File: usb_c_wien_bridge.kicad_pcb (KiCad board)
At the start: 2 copper layers, 49 x 14 mm, 20 parts, among them J1 USB_C_Receptacle_USB2.0, J2 Conn_01x05_Female, U1 TL082

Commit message: Place all components. Needs routing.
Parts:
- added C10: 47uF, Capacitor_SMD:CP_Elec_6.3x5.4_Nichicon, F.Cu at (193.0, 17.8)
- added C11: 1uF, Capacitor_SMD:C_0603_1608Metric_Pad1.05x0.95mm_HandSolder, B.Cu at (183.1, 22.0)
- added C12: 1uF, Capacitor_SMD:C_0603_1608Metric_Pad1.05x0.95mm_HandSolder, B.Cu at (183.1, 20.4)
- added C9: 1nF, Capacitor_SMD:C_0603_1608Metric_Pad1.05x0.95mm_HandSolder, B.Cu at (185.3, 13.5)
- added J3: Conn_02x02, Connector_PinSocket_2.00mm:PinSocket_2x02_P2.00mm_Horizontal, F.Cu at (177.8, 20.9)
- added U2: MIC5504-3.3YM5, Package_TO_SOT_SMD:SOT-23-5, B.Cu at (171.6, 17.1)
- C1, C2, D1, D2, R1, R2, R3, R4, R5, R6, R7: moved to B.Cu
- C3: value 0u1F -> 1uF; footprint Capacitor_SMD:C_0603_1608Metric -> Capacitor_SMD:C_0603_1608Metric_Pad1.05x0.95mm_HandSolder; moved to B.Cu
- C4: footprint Capacitor_SMD:C_0603_1608Metric_Pad1.05x0.95mm_HandSolder -> Capacitor_SMD:C_0603_1608Metric; moved to B.Cu
- C5: value 1nF -> 0u1F; moved to B.Cu
- C6: value 1nF -> 1uF; moved to B.Cu
- C7: value 47uF -> 0u1F; footprint Capacitor_SMD:CP_Elec_6.3x5.4_Nichicon -> Capacitor_SMD:C_0603_1608Metric; moved to B.Cu
- C8: value 1uF -> 1nF; moved to B.Cu
- J1: footprint Connector_USB:USB_C_Receptacle_Amphenol_12401610E4-2A -> Amphenol:USB_C_Receptacle_Amphenol_12401610E4-2A
- J2: value Conn_01x05_Female -> Screw_Terminal_01x02; footprint Connector_PinSocket_2.54mm:PinSocket_1x05_P2.54mm_Horizontal -> TerminalBlock_TE-Connectivity:TerminalBlock_TE_282834-2_1x02_P2.54mm_Horizontal
- U1: value TL082 -> LMV358; footprint Package_SO:SOIC-8_3.9x4.9mm_P1.27mm -> Package_SO:TSSOP-8_4.4x3mm_P0.65mm; moved to B.Cu
- moved C4 154.2 mm to (169.3, 20.6), turned to 270 degrees
- moved C6 146.7 mm to (171.8, 19.8), turned to 180 degrees
- moved C5 140.4 mm to (186.1, 21.5), turned to 270 degrees
- moved R2 134.5 mm to (179.1, 16.9), turned to 180 degrees
- moved C3 134.0 mm to (187.7, 21.5), turned to 270 degrees
- moved R4 133.5 mm to (185.3, 15.1), turned to 180 degrees
- moved R1 132.8 mm to (179.1, 18.5)
- moved C1 131.3 mm to (189.4, 21.5), turned to 270 degrees
- moved D1 131.2 mm to (193.2, 17.7), turned to 270 degrees
- moved R3 130.1 mm to (191.1, 14.2), turned to 90 degrees
- moved C8 129.2 mm to (187.8, 14.2), turned to 270 degrees
- moved R6 125.4 mm to (189.5, 14.2), turned to 90 degrees
- moved C2 125.2 mm to (168.8, 17.3), turned to 90 degrees
- moved R7 122.8 mm to (191.0, 22.5), turned to 270 degrees
- moved R5 122.3 mm to (189.9, 17.7), turned to 90 degrees
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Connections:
- net Net-(D1-Pad1) renamed /NEG_FB
- C1 pad 1: +5V0 -> +3V3
- C3 pad 1: +5V0 -> +3V3
- C4 pad 1: Net-(C4-Pad1) -> +5V0
- C5 pad 1: Net-(C5-Pad1) -> /V_DIV
- C5 pad 2: Net-(C5-Pad2) -> GNDA
- C6 pad 1: /RAIL_SPLIT -> +3V3
- C6 pad 2: Net-(C5-Pad2) -> GNDA
- C7 pad 1: Net-(C7-Pad1) -> +3V3
- C7 pad 2: Net-(C7-Pad2) -> GNDA
- C8 pad 1: +5V0 -> Net-(C8-Pad1)
- C8 pad 2: GNDA -> /POS_FB
- D1 pad 2: Net-(C7-Pad1) -> Net-(C10-Pad1)
- D2 pad 1: Net-(C7-Pad1) -> Net-(C10-Pad1)
- J1 pad A5: (no net) -> Net-(J1-PadA5)
- J1 pad A6: (no net) -> Net-(J1-PadA6)
- J1 pad A7: (no net) -> Net-(J1-PadA7)
- J1 pad A8: (no net) -> Net-(J1-PadA8)
- J1 pad B5: (no net) -> Net-(J1-PadB5)
- J1 pad B6: (no net) -> Net-(J1-PadB6)
- J1 pad B7: (no net) -> Net-(J1-PadB7)
- J1 pad B8: (no net) -> Net-(J1-PadB8)
- J2 pad 1: GNDA -> Net-(J2-Pad1)
- J2 pad 2: Net-(C7-Pad2) -> +5V0
- R1 pad 1: +5V0 -> +3V3
- R1 pad 2: Net-(C4-Pad1) -> /V_DIV
- R2 pad 1: Net-(C4-Pad1) -> /V_DIV
- R4 pad 1: Net-(C5-Pad2) -> /POS_FB
- R5 pad 1: Net-(C7-Pad1) -> Net-(C10-Pad1)
- R6 pad 1: Net-(C7-Pad1) -> Net-(C10-Pad1)
- R6 pad 2: Net-(C5-Pad1) -> Net-(C8-Pad1)
- R7 pad 1: Net-(C7-Pad2) -> /A_OUT
- U1 pad 2: Net-(C4-Pad1) -> /RAIL_SPLIT
- U1 pad 3: GNDA -> /V_DIV
- U1 pad 5: Net-(C5-Pad2) -> /POS_FB
- U1 pad 7: Net-(C7-Pad1) -> Net-(C10-Pad1)
- U1 pad 8: +5V0 -> +3V3
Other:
- board size 49 x 14 mm -> 31.8 x 12.7 mm

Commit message: Finish routing
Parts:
- R7: moved to F.Cu
- moved C10 91.8 mm to (146.7, 97.0), turned to 180 degrees
- moved R7 91.4 mm to (137.4, 96.5), turned to 180 degrees
- moved C12 89.5 mm to (142.7, 100.3)
- moved J3 87.9 mm to (137.4, 99.0)
- moved C2 87.9 mm to (128.4, 95.4)
- moved C4 87.9 mm to (128.9, 98.7)
- moved C6 87.9 mm to (131.4, 97.9)
- moved J1 87.9 mm to (129.8, 95.9)
- moved J2 87.9 mm to (140.6, 91.8)
- moved R1 87.9 mm to (138.7, 96.6)
- moved R4 87.9 mm to (144.9, 93.2)
- moved U1 87.9 mm to (144.7, 95.9)
- moved U2 87.9 mm to (131.2, 95.2)
- moved C1 87.9 mm to (149.0, 99.6)
- moved C3 87.9 mm to (147.3, 99.6)
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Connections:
- J3 pad 1: GNDA -> /A_OUT
- J3 pad 2: /A_OUT -> GNDA
- J3 pad 3: +3V3 -> +5V0
- J3 pad 4: +5V0 -> +3V3
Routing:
- net +3V3: track 0.00 -> 36.0 mm
- net GNDA: track 0.00 -> 31.9 mm, vias 0 -> 8
- net +5V0: track 0.00 -> 31.6 mm, vias 0 -> 2
- net Net-(C10-Pad1): track 0.00 -> 22.2 mm, vias 0 -> 2
- net /RAIL_SPLIT: track 0.00 -> 14.7 mm
- net Net-(J2-Pad1): track 0.00 -> 13.7 mm
- net /V_DIV: track 0.00 -> 10.8 mm
- net /A_OUT: track 0.00 -> 8.55 mm
- net /NEG_FB: track 0.00 -> 7.18 mm
- net /POS_FB: track 0.00 -> 5.09 mm
- net Net-(C8-Pad1): track 0.00 -> 1.65 mm
- added copper zone on B.Cu, net GNDA
- added copper zone on F.Cu, net GNDA
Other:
- net class OSH Park Minimums added: clearance 0.1524, trace_width 0.1524, via_dia 0.508, via_drill 0.254
- rule pad_to_mask_clearance: 0.051 -> 0.0508
- rule solder_mask_min_width: 0.25 -> 0.1016
- rule trace_min: 0.2 -> 0.1524
- rule via_min_drill: 0.3 -> 0.254
- rule via_min_size: 0.4 -> 0.508

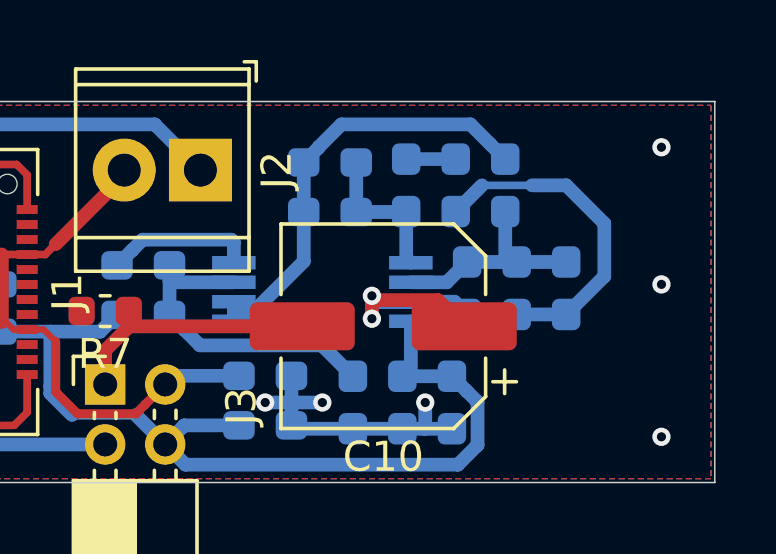
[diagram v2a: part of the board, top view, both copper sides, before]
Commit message: Add vias to ground islands
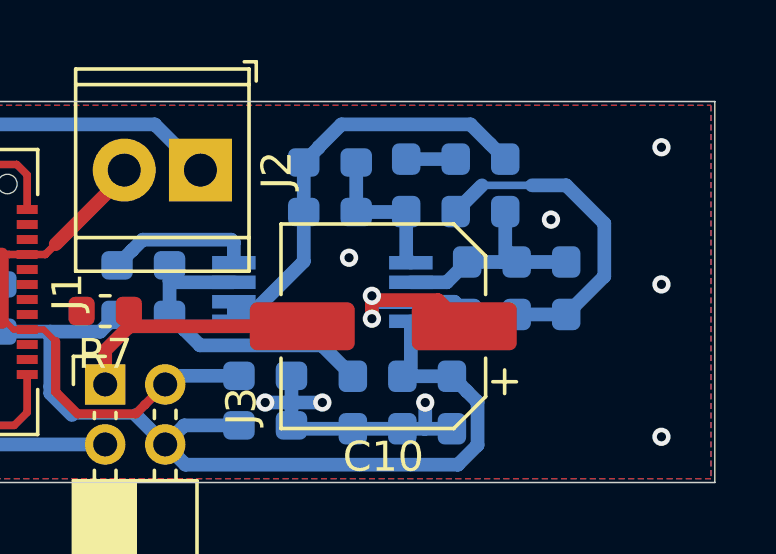
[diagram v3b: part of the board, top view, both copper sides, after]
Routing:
- net GNDA: vias 8 -> 10
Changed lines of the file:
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@@
     (thickness 1.6)
     (drawings 4)
-    (tracks 177)
+    (tracks 179)
     (zones 0)
     (modules 26)
@@
   )
   (setup
-    (last_trace_width 0.3048)
+    (last_trace_width 0.25)
     (user_trace_width 0.1524)
     (user_trace_width 0.2032)
@@
   (gr_line (start 157.734 89.535) (end 157.734 102.235) (layer Edge.Cuts) (width 0.05))
   (gr_line (start 125.984 89.535) (end 157.734 89.535) (layer Edge.Cuts) (width 0.05))
+  (via (at 152.273 93.472) (size 0.6096) (drill 0.3048) (layers F.Cu B.Cu) (net 1))
+  (via (at 145.542 94.742) (size 0.6096) (drill 0.3048) (layers F.Cu B.Cu) (net 1))
   (via (at 128.397 93.345) (size 0.6096) (drill 0.3048) (layers F.Cu B.Cu) (net 1))
   (via (at 127.254 94.488) (size 0.6096) (drill 0.3048) (layers F.Cu B.Cu) (net 1))
@@
   (via (at 131.191 94.869) (size 0.6096) (drill 0.3048) (layers F.Cu B.Cu) (net 2))
   (via (at 131.191 95.631) (size 0.6096) (drill 0.3048) (layers F.Cu B.Cu) (net 2))
-  (via (at 146.304 96.774) (size 0.6096) (drill 0.3048) (layers F.Cu B.Cu) (net 6))
-  (via (at 146.304 96.012) (size 0.6096) (drill 0.3048) (layers F.Cu B.Cu) (net 6))
   (segment (start 130.025 96.266) (end 130.091 96.2) (width 0.4572) (layer B.Cu) (net 2))
   (segment (start 128.905 97.8915) (end 128.905 96.266) (width 0.4572) (layer B.Cu) (net 2))
@@
   (segment (start 138.434199 99.985199) (end 136.307199 99.985199) (width 0.3048) (layer B.Cu) (net 4))
   (segment (start 149.098 91.454) (end 147.447 91.454) (width 0.4572) (layer B.Cu) (net 5))
+  (via (at 146.304 96.774) (size 0.6096) (drill 0.3048) (layers F.Cu B.Cu) (net 6))
+  (via (at 146.304 96.012) (size 0.6096) (drill 0.3048) (layers F.Cu B.Cu) (net 6))
   (segment (start 149.056 96.21) (end 149.479 96.633) (width 0.4572) (layer B.Cu) (net 6))
   (segment (start 147.603 96.21) (end 149.056 96.21) (width 0.4572) (layer B.Cu) (net 6))

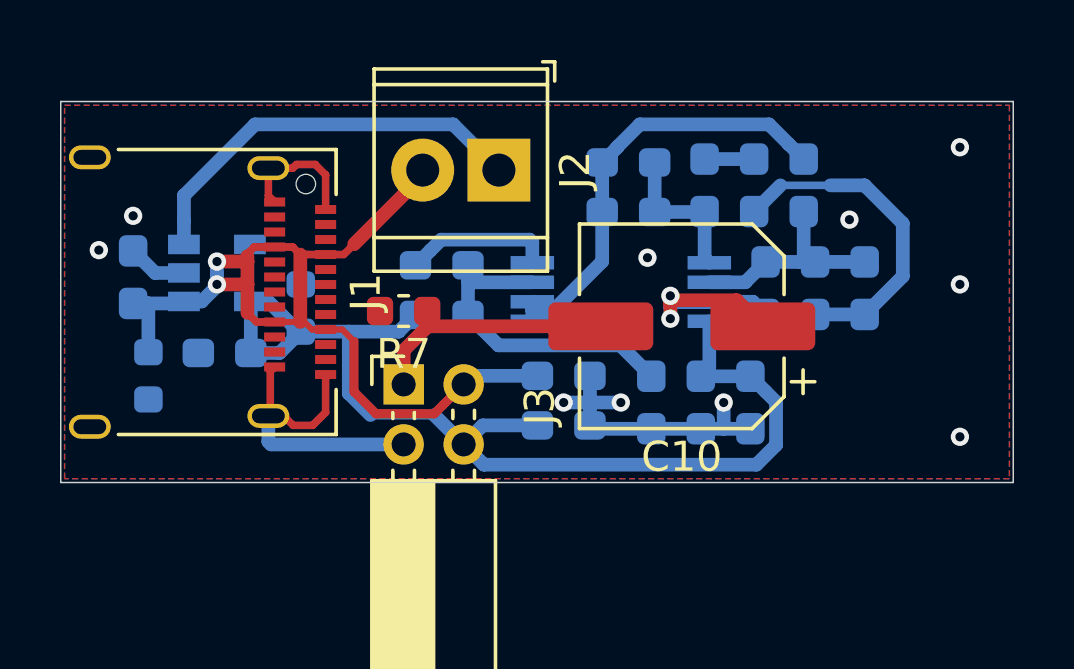
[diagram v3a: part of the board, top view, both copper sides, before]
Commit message: * 10 mil fillet edge cuts corners * 10 mil fillet  front and back GND zones * Shrink board
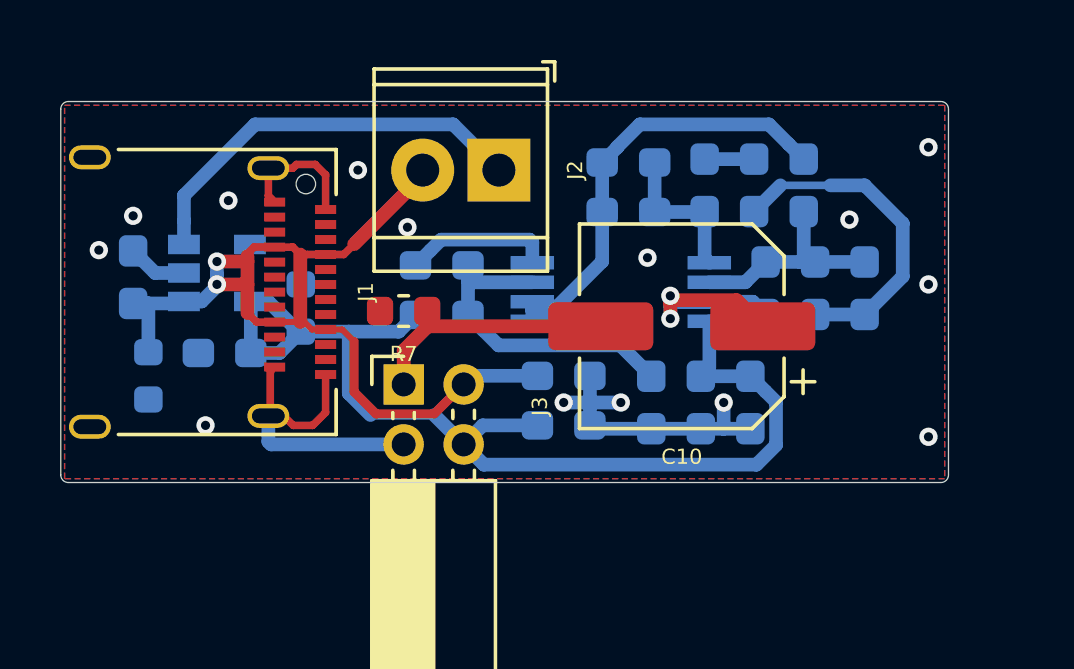
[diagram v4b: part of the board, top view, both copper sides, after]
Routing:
- net GNDA: vias 10 -> 14
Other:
- board size 31.8 x 12.7 mm -> 29.6 x 12.7 mm

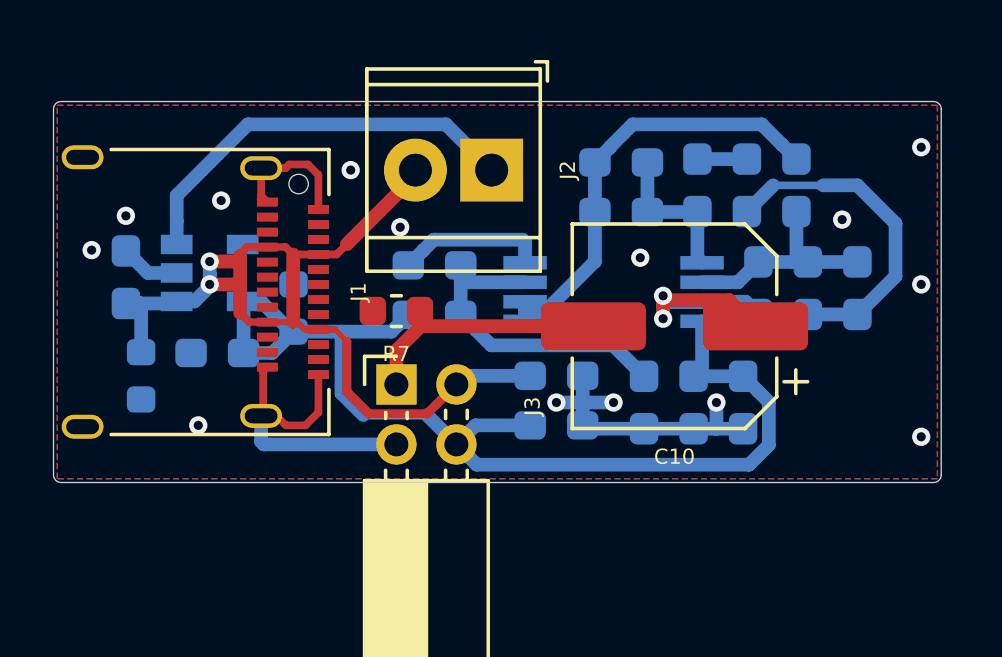
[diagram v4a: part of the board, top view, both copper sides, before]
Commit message: Fix silkcsreen designator sizes and position
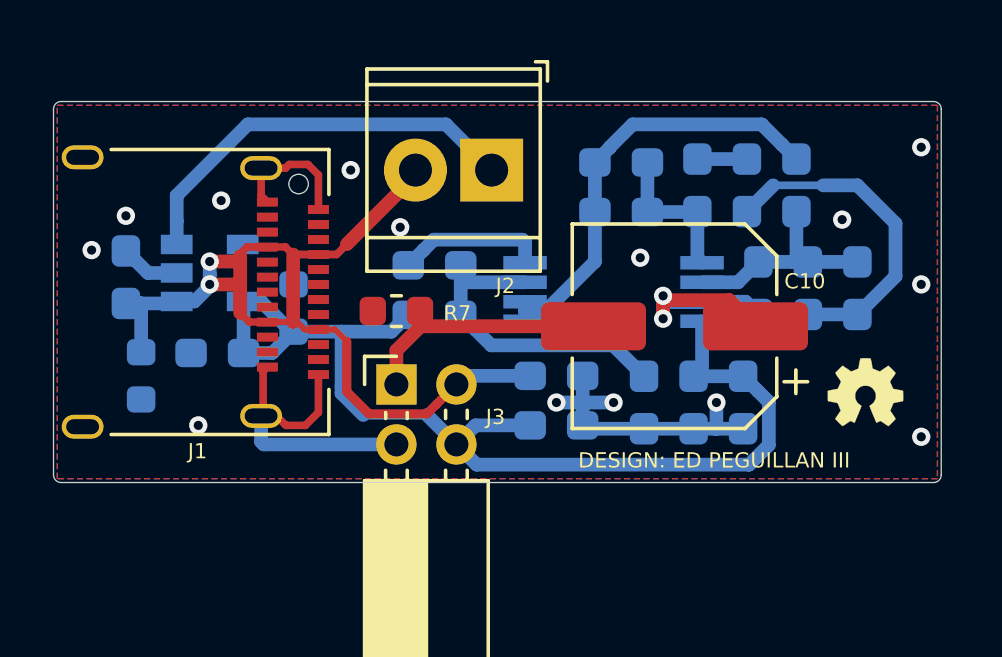
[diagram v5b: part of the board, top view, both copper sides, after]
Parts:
- added G***: LOGO, Symbol:OSHW-Symbol_2.6x2.3mm_SilkScreen, F.Cu at (153.0, 99.2)
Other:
- board text added: "DESIGN: ED PEGUILLAN III"
- board text added: "HAPPY BIRTHDAY KATRINA SCHROEDER :)"
- board text added: "~~700 Hz WIEN BRIDGE OSCILLATOR"

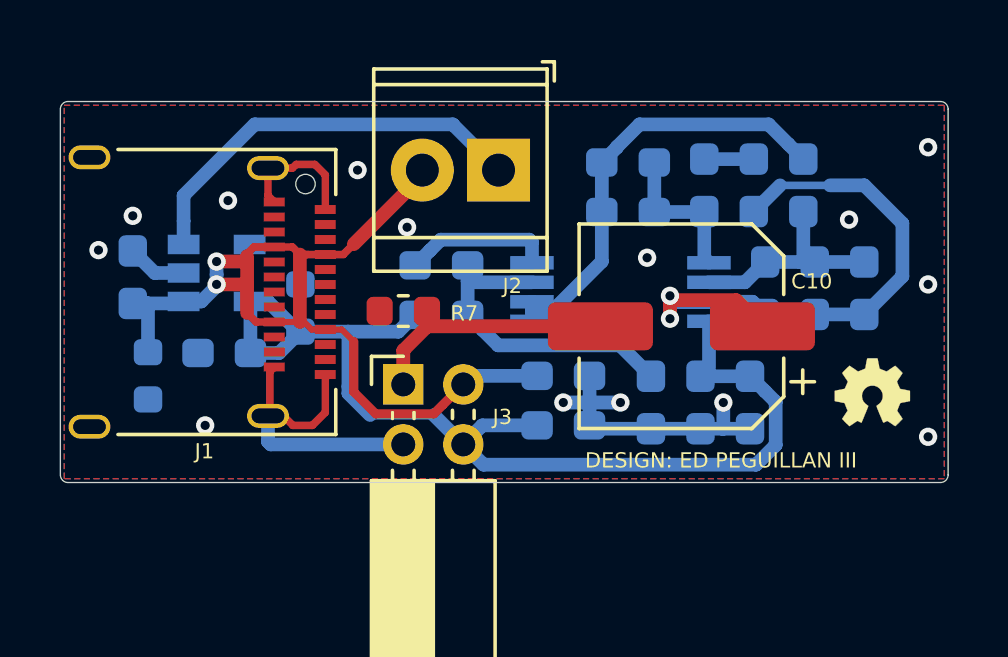
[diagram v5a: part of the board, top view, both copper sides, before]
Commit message: Add revision number to PCB
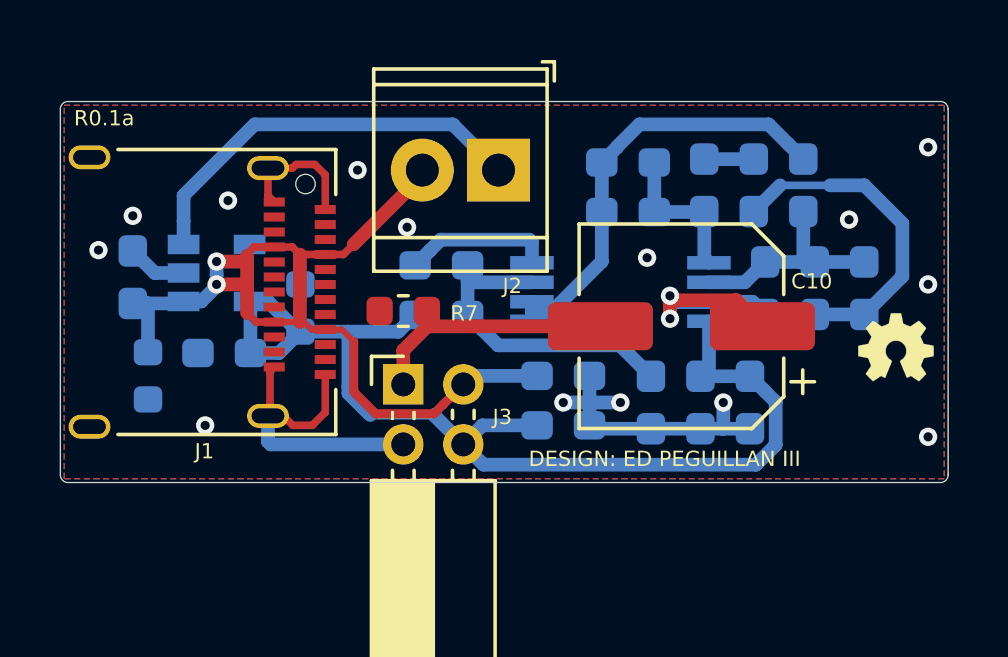
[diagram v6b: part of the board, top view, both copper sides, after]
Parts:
- moved G*** 1.69 mm to (153.8, 97.7)
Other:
- board text added: "R0.1a"
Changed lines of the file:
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@@
   (general
     (thickness 1.6)
-    (drawings 11)
+    (drawings 12)
     (tracks 183)
     (zones 0)
@@
   (page USLetter)
   (title_block
+    (title "~~700 Hz WIEN BRIDGE OSCILLATOR")
     (date 2019-03-31)
+    (rev 0.1a)
   )
   (layers
@@
   )
   (module Symbol:OSHW-Symbol_2.6x2.3mm_SilkScreen (layer F.Cu)
-    (at 153.0477 99.2251)
+    (at 153.8351 97.7265)
     (fp_text reference G*** (at 0 0) (layer F.SilkS) hide
       (effects (font (size 1.524 1.524) (thickness 0.3)))
@@
     )
   )
-  (gr_text "DESIGN: ED PEGUILLAN III" (at 148.0058 101.4984) (layer F.SilkS)
+  (gr_text R0.1a (at 127.4445 90.0938) (layer F.SilkS)
     (effects (font (size 0.508 0.508) (thickness 0.127)))
   )
+  (gr_text "DESIGN: ED PEGUILLAN III" (at 146.1262 101.4476) (layer F.SilkS)
+    (effects (font (size 0.508 0.508) (thickness 0.127)))
+  )
